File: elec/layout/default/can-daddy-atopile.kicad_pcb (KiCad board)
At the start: 2 copper layers, 225.7 x 100.8 mm, 0 parts

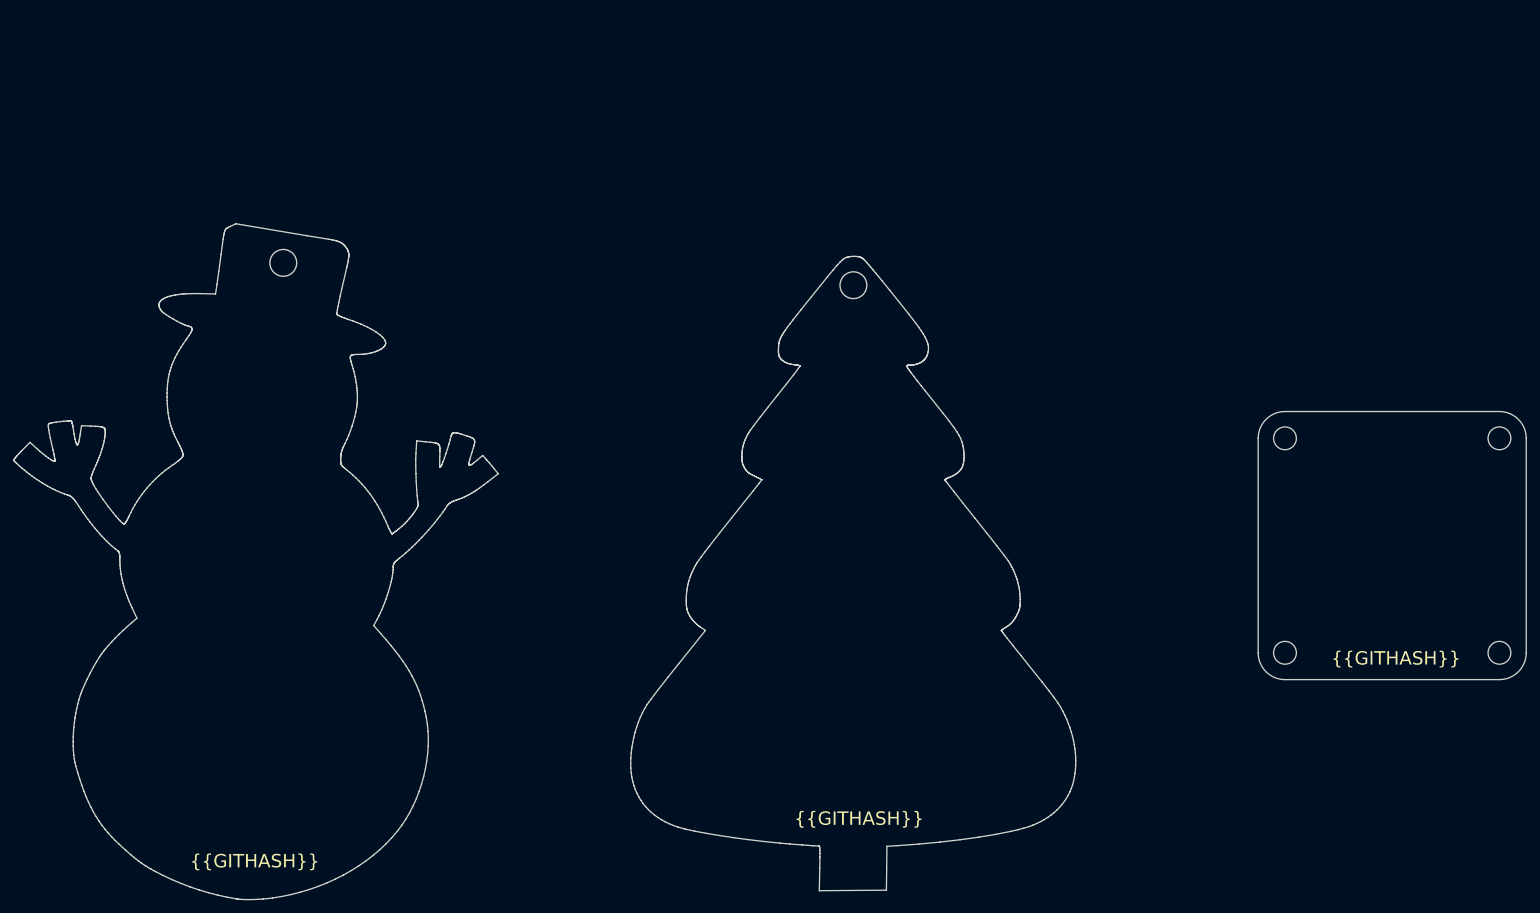
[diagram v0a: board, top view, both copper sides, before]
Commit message: Adding in revisions 2 and 3
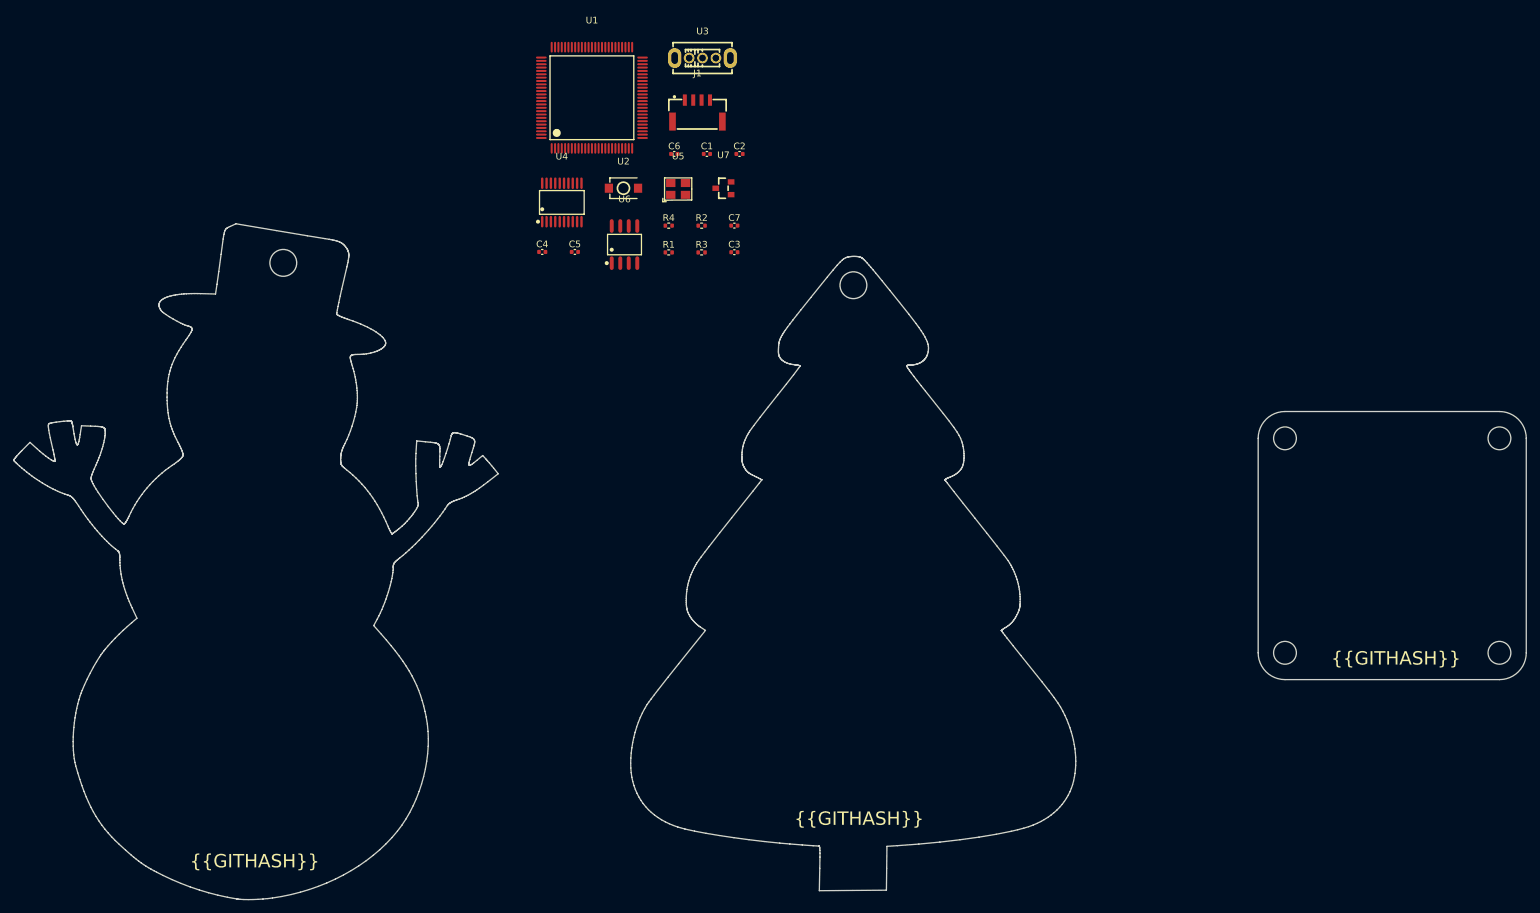
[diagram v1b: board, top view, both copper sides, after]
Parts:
- added C1: 16V 100nF X7R ±10% 0402 Multilayer Ceramic Capacitors MLCC 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, lib:C0402, F.Cu at (139.4, 39.4)
- added C2: 50V 9pF C0G 0402 Multilayer Ceramic Capacitors MLCC - SMD/S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, lib:C0402, F.Cu at (144.2, 39.4)
- added C3: 50V 9pF C0G 0402 Multilayer Ceramic Capacitors MLCC - SMD/S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, lib:C0402, F.Cu at (143.5, 54.0)
- added C4: 16V 100nF X7R ±10% 0402 Multilayer Ceramic Capacitors MLCC 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, lib:C0402, F.Cu at (114.8, 54.0)
- added C5: 16V 100nF X7R ±10% 0402 Multilayer Ceramic Capacitors MLCC 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, lib:C0402, F.Cu at (119.7, 54.0)
- added C6: 25V 47nF X7R ±10% 0402 Multilayer Ceramic Capacitors MLCC -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, lib:C0402, F.Cu at (134.5, 39.4)
- added C7: 25V 47nF X7R ±10% 0402 Multilayer Ceramic Capacitors MLCC -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, lib:C0402, F.Cu at (143.5, 50.0)
- added J1: , lib:CONN-SMD_4P-P1.25_SM04B-GHS-TB-LF-SN, F.Cu at (138.0, 32.9)
- added R1: 62.5mW Thick Film Resistors 50V ±100ppm/℃ ±1% 4.7kΩ 0402 Ch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, lib:R0402, F.Cu at (133.7, 54.0)
- added R2: 62.5mW Thick Film Resistors 50V ±100ppm/℃ ±1% 4.7kΩ 0402 Ch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, lib:R0402, F.Cu at (138.6, 50.1)
- added R3: 62.5mW Thick Film Resistors 50V ±100ppm/℃ ±1% 10kΩ 0402 Chi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, lib:R0402, F.Cu at (138.6, 54.0)
- added R4: 62.5mW Thick Film Resistors 50V ±100ppm/℃ ±1% 120Ω 0402 Chi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, lib:R0402, F.Cu at (133.7, 50.1)
- added U1: , lib:LQFP-100_L14.0-W14.0-P0.50-LS16.0-BL, F.Cu at (122.2, 31.0)
- added U2: , lib:SW-SMD_L3.9-W3.0-P4.45, F.Cu at (126.9, 44.5)
- added U3: , lib:SW-TH_SS12D07VG4, F.Cu at (138.7, 25.1)
- added U4: , lib:TSSOP-20_L6.5-W4.4-P0.65-LS6.4-BL, F.Cu at (117.7, 46.6)
- added U5: , lib:OSC-SMD_4P-L3.2-W2.5-BL, F.Cu at (135.1, 44.6)
- added U6: , lib:SOIC-8_L4.9-W3.9-P1.27-LS6.0-BL, F.Cu at (127.1, 52.9)
- added U7: , lib:SOT-23_L2.9-W1.3-P1.90-LS2.4-BR, F.Cu at (141.8, 44.5)
